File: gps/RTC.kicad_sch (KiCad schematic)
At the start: 15 parts, among them U10 M24C01-FMN, U9 DS3231M

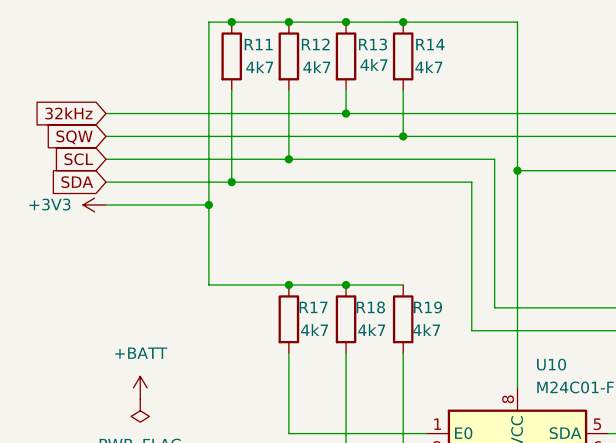
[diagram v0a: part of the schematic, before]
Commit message: update pcd/sch
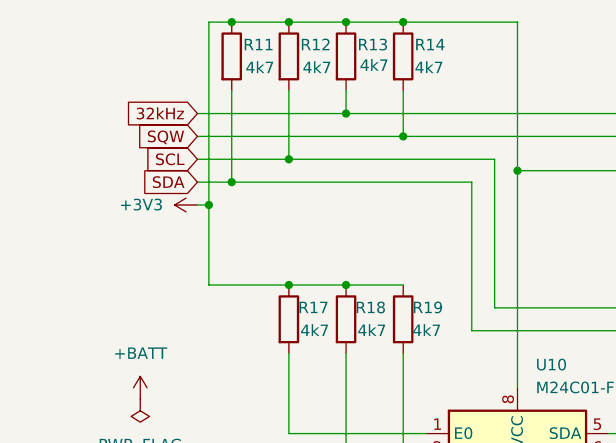
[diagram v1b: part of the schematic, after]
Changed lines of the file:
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@@
 	(wire
 		(pts
-			(xy 90.17 74.93) (xy 116.84 74.93)
+			(xy 100.33 74.93) (xy 116.84 74.93)
 		)
 		(stroke
@@
 	(wire
 		(pts
-			(xy 90.17 85.09) (xy 101.6 85.09)
+			(xy 100.33 85.09) (xy 101.6 85.09)
 		)
 		(stroke
@@
 	(wire
 		(pts
-			(xy 90.17 77.47) (xy 123.19 77.47)
+			(xy 100.33 77.47) (xy 123.19 77.47)
 		)
 		(stroke
@@
 	(wire
 		(pts
-			(xy 90.17 82.55) (xy 104.14 82.55)
+			(xy 100.33 82.55) (xy 104.14 82.55)
 		)
 		(stroke
@@
 	(wire
 		(pts
-			(xy 90.17 80.01) (xy 110.49 80.01)
+			(xy 100.33 80.01) (xy 110.49 80.01)
 		)
 		(stroke
@@
 	(global_label "SCL"
 		(shape input)
-		(at 90.17 80.01 180)
+		(at 100.33 80.01 180)
 		(fields_autoplaced yes)
 		(effects
@@
 		)
 		(property "Intersheetrefs" "${INTERSHEET_REFS}"
-			(at 84.2493 79.9306 0)
+			(at 94.4093 79.9306 0)
 			(effects
 				(font
@@
 	(global_label "SDA"
 		(shape input)
-		(at 90.17 82.55 180)
+		(at 100.33 82.55 180)
 		(fields_autoplaced yes)
 		(effects
@@
 		)
 		(property "Intersheetrefs" "${INTERSHEET_REFS}"
-			(at 84.1888 82.4706 0)
+			(at 94.3488 82.4706 0)
 			(effects
 				(font
@@
 	(global_label "SQW"
 		(shape input)
-		(at 90.17 77.47 180)
+		(at 100.33 77.47 180)
 		(fields_autoplaced yes)
 		(effects
@@
 		)
 		(property "Intersheetrefs" "${INTERSHEET_REFS}"
-			(at 83.1934 77.47 0)
+			(at 93.3534 77.47 0)
 			(effects
 				(font
@@
 	(global_label "32kHz"
 		(shape input)
-		(at 90.17 74.93 180)
+		(at 100.33 74.93 180)
 		(fields_autoplaced yes)
 		(effects
@@
 		)
 		(property "Intersheetrefs" "${INTERSHEET_REFS}"
-			(at 81.9512 74.8506 0)
+			(at 92.1112 74.8506 0)
 			(effects
 				(font
@@
 	(symbol
 		(lib_id "power:+3V3")
-		(at 90.17 85.09 90)
+		(at 100.33 85.09 90)
 		(unit 1)
 		(exclude_from_sim no)
@@
 		(fields_autoplaced yes)
 		(property "Reference" "#PWR047"
-			(at 93.98 85.09 0)
+			(at 104.14 85.09 0)
 			(effects
 				(font
@@
 		)
 		(property "Value" "+3V3"
-			(at 86.36 85.0899 90)
+			(at 96.52 85.0899 90)
 			(effects
 				(font
@@
 		)
 		(property "Footprint" ""
-			(at 90.17 85.09 0)
+			(at 100.33 85.09 0)
 			(effects
 				(font
@@
 		)
 		(property "Datasheet" ""
-			(at 90.17 85.09 0)
+			(at 100.33 85.09 0)
 			(effects
 				(font
@@
 		)
 		(property "Description" "Power symbol creates a global label with name \"+3V3\""
-			(at 90.17 85.09 0)
-			(effects
-				(font
+			(at 100.33 85.09 0)
+			(effects
+				(font

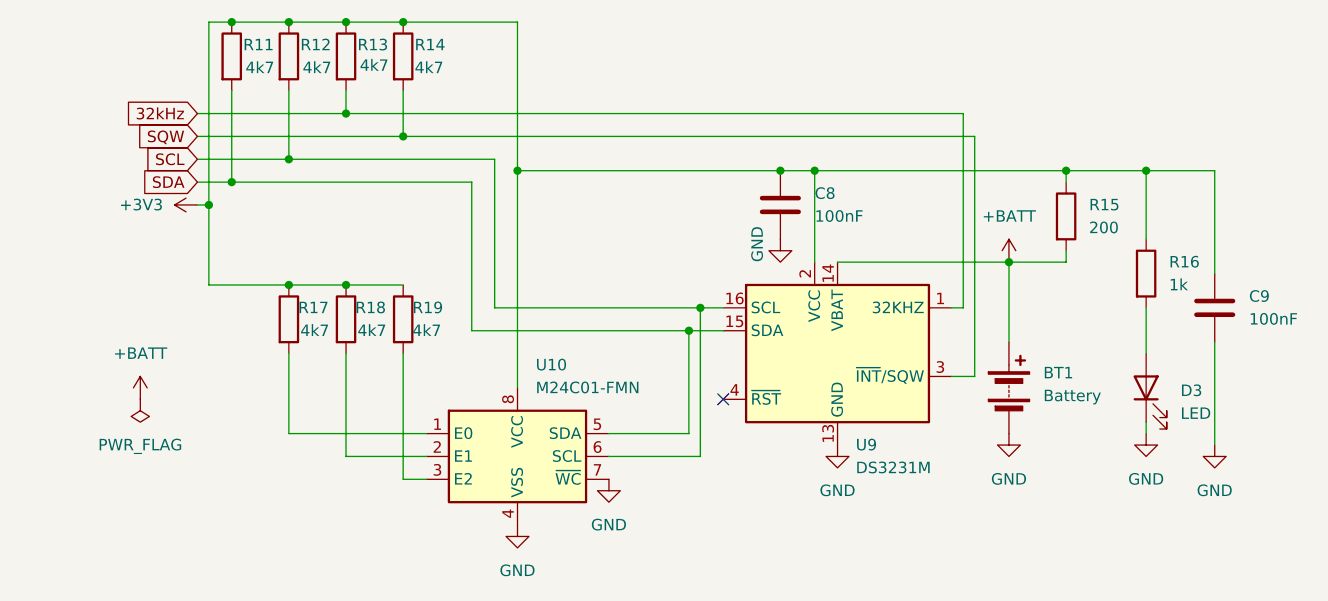
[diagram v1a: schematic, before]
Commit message: update pcb/housing
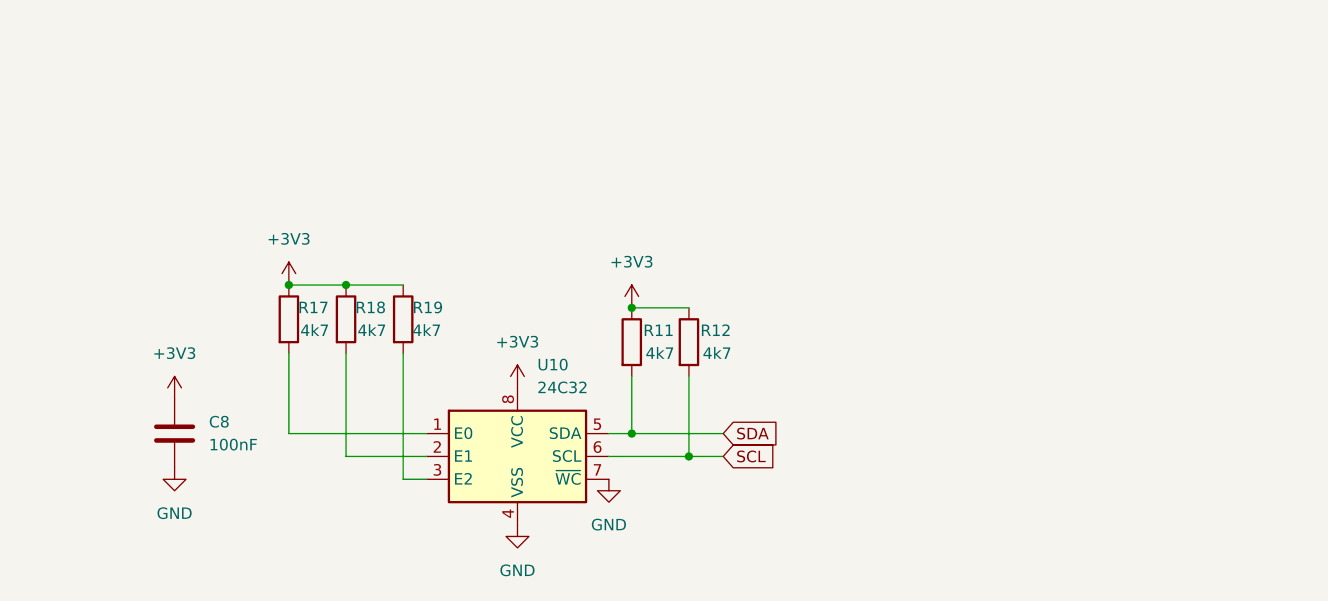
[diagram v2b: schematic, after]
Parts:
- removed BT1: Battery, Battery:BatteryHolder_Keystone_107_1x23mm, symbol Device:Battery
- removed C9: 100nF, Capacitor_SMD:C_0805_2012Metric_Pad1.18x1.45mm_HandSolder, symbol Device:C
- removed D3: LED, LED_SMD:LED_0805_2012Metric_Pad1.15x1.40mm_HandSolder, symbol Device:LED
- removed R13, R14: 4k7, Resistor_SMD:R_0805_2012Metric_Pad1.20x1.40mm_HandSolder, symbol Device:R
- removed R15: 200, Resistor_SMD:R_0805_2012Metric_Pad1.20x1.40mm_HandSolder, symbol Device:R
- removed R16: 1k, Resistor_SMD:R_0805_2012Metric_Pad1.20x1.40mm_HandSolder, symbol Device:R
- removed U9: DS3231M, Package_SO:SOIC-16W_7.5x10.3mm_P1.27mm, symbol Timer_RTC:DS3231M
- U10: value M24C01-FMN -> 24C32
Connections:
- no-connect marks 1 -> 0
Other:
- moved on the sheet: C8, R11, R12

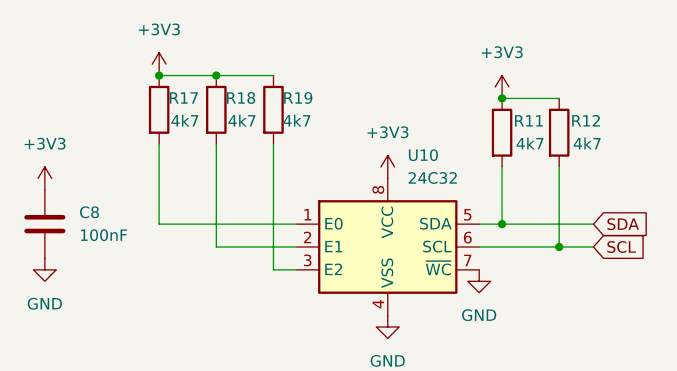
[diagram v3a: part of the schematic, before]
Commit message: changed eeprom > 5V, RF antenna track corrected to 50ohm
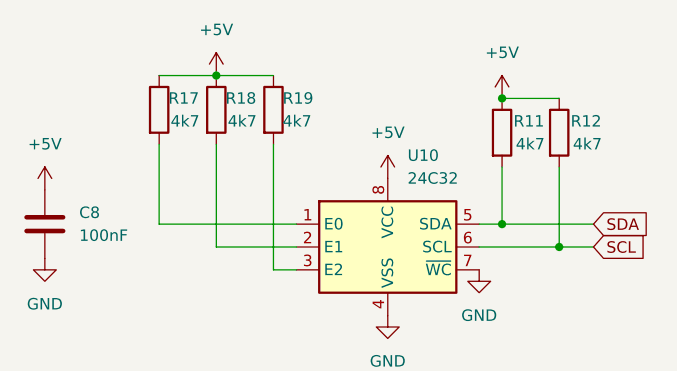
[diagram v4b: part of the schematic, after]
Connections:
- net +3V3 renamed +5V

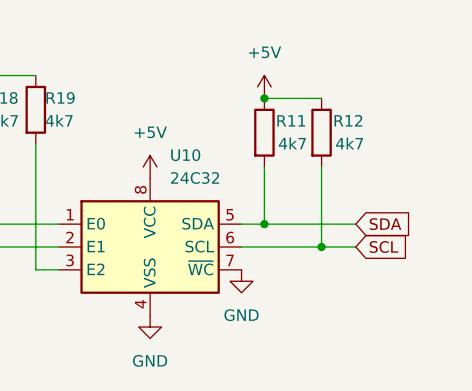
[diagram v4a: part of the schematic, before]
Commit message: added level shifters for i2C and RGB displey,
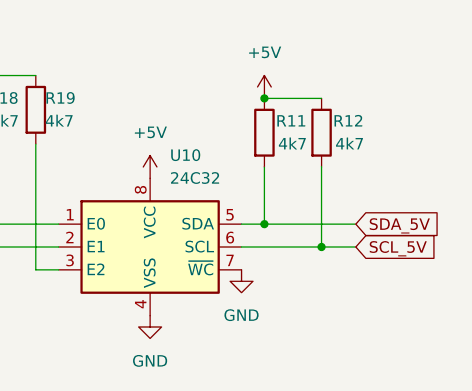
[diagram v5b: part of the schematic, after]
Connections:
- net SCL renamed SCL_5V
- net SDA renamed SDA_5V
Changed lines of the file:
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@@
 		)
 	)
-	(global_label "SCL"
+	(global_label "SCL_5V"
 		(shape input)
 		(at 158.75 113.03 0)
@@
 		)
 		(property "Intersheetrefs" "${INTERSHEET_REFS}"
-			(at 165.2428 113.03 0)
+			(at 168.5085 113.03 0)
 			(effects
 				(font
@@
 		)
 	)
-	(global_label "SDA"
+	(global_label "SDA_5V"
 		(shape input)
 		(at 158.75 110.49 0)
@@
 		)
 		(property "Intersheetrefs" "${INTERSHEET_REFS}"
-			(at 165.3033 110.49 0)
+			(at 168.569 110.49 0)
 			(effects
 				(font

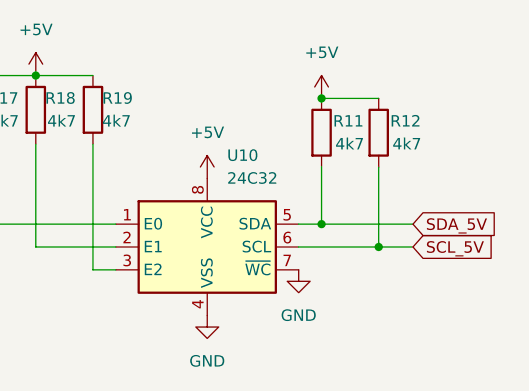
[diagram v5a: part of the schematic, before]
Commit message: added pullup for 3V3 i2c
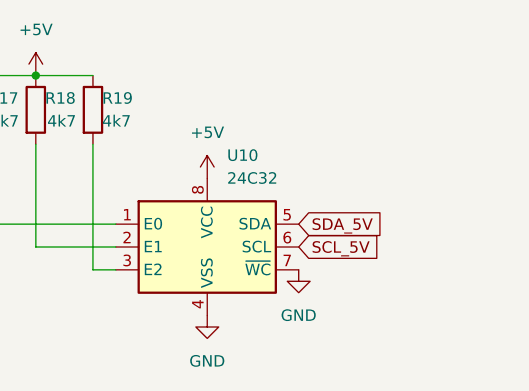
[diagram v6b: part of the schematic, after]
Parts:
- removed R11, R12: 4k7, Resistor_SMD:R_0805_2012Metric_Pad1.20x1.40mm_HandSolder, symbol Device:R

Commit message: cleaned schematic
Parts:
- removed C8: 100nF, Capacitor_SMD:C_0805_2012Metric_Pad1.18x1.45mm_HandSolder, symbol Device:C
- removed R17, R18, R19: 4k7, Resistor_SMD:R_0805_2012Metric_Pad1.20x1.40mm_HandSolder, symbol Device:R
- removed U10: 24C32, Package_SO:SOIC-8_3.9x4.9mm_P1.27mm, symbol Memory_EEPROM:M24C01-FMN
